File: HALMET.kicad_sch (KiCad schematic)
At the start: 0 parts

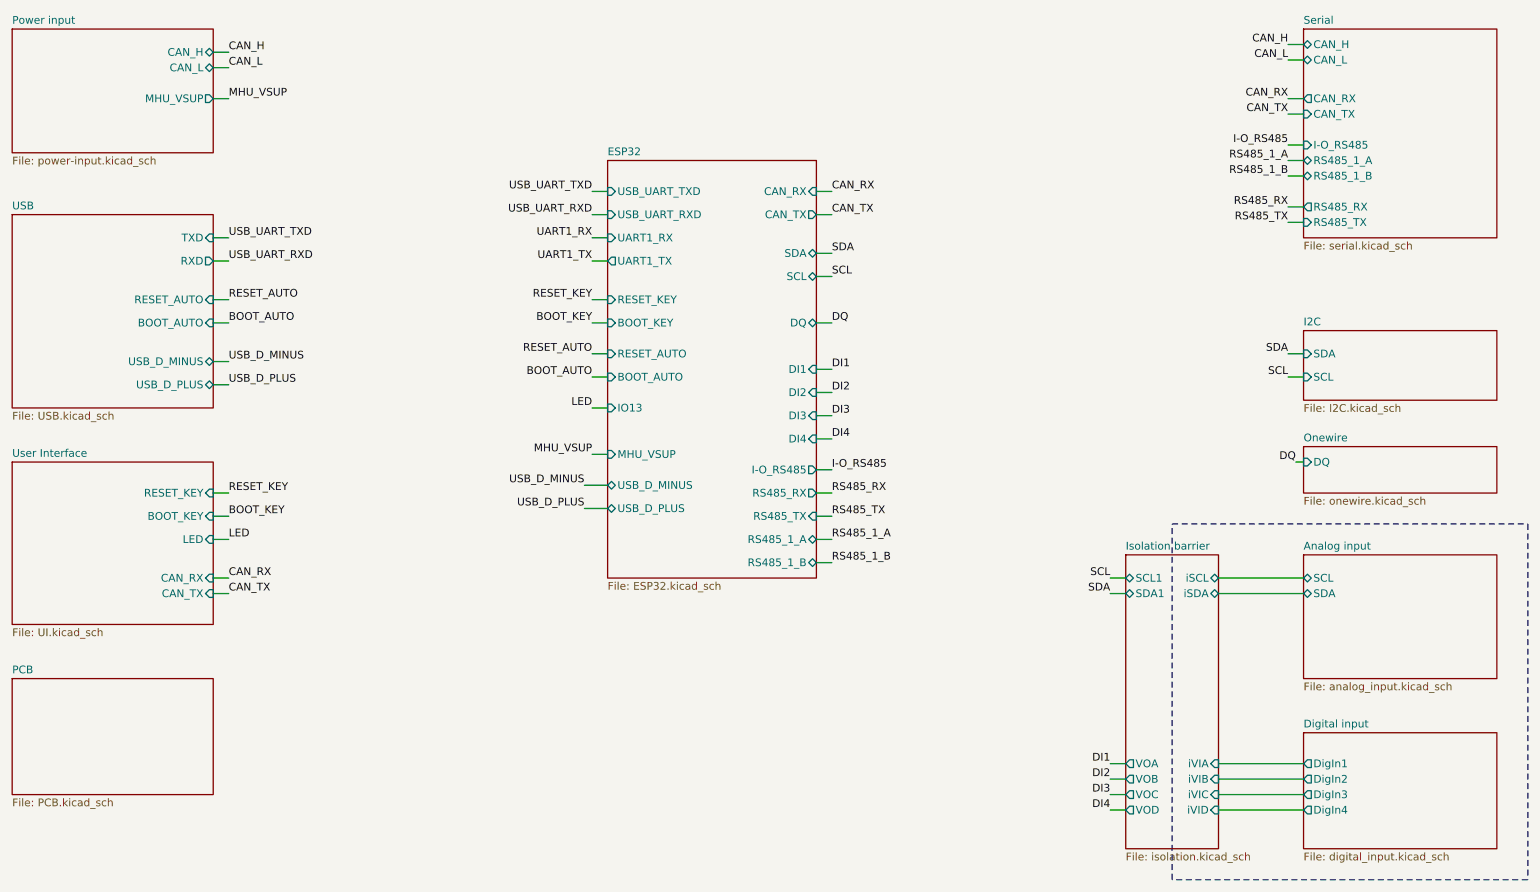
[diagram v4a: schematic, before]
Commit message: Net renaming and Silkscreen tidy ups
The UART / Serial naming convention is revised for more consistency
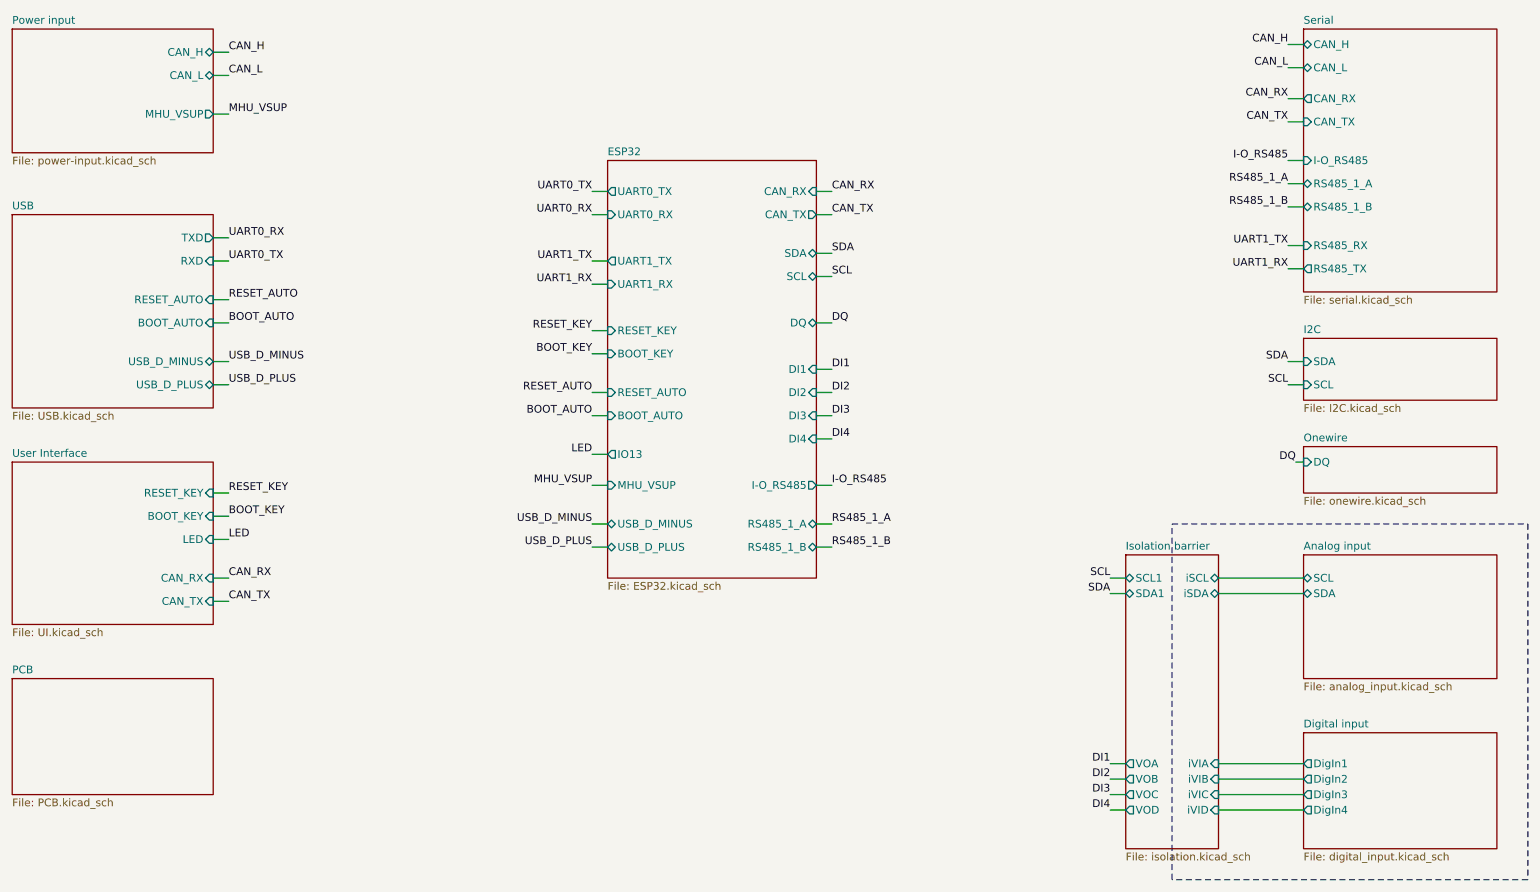
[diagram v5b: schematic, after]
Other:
- sheet ESP32 ports: added UART0_RX, UART0_TX; removed RS485_RX, RS485_TX, USB_UART_RXD, USB_UART_TXD

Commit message: Moved ESP32-S3 + larger pin headers
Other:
- company: Hat Labs Ltd -> Fifty One North Limited
- title: Hat Labs Marine Engine & Tank interface (HALMET) -> Bluefin Marine Processor
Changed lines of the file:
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@@
 	(paper "A4")
 	(title_block
-		(title "Hat Labs Marine Engine & Tank interface (HALMET)")
-		(date "2024-01-18")
-		(rev "1.0.1")
-		(company "Hat Labs Ltd")
-		(comment 1 "https://creativecommons.org/licenses/by-sa/4.0")
-		(comment 2 "To view a copy of this license, visit ")
-		(comment 3 "HALMET is licensed under CC BY-SA 4.0.")
+		(title "Bluefin Marine Processor")
+		(date "2026-01-08")
+		(rev "1.0.0")
+		(company "Fifty One North Limited")
+		(comment 1 "https://creativecommons.org/licenses/by-sa/4.0/")
+		(comment 2 "Bluefin is licensed under CC BY-SA 4.0")
+		(comment 3 "Modifications © 2026 Fiftyone North Ltd.")
+		(comment 4 "Based on an original design by Hat Labs Ltd.")
 	)
 	(rectangle
